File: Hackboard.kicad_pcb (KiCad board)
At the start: 4 copper layers, 110.2 x 55.9 mm, 74 parts, among them J1 Conn_01x31_Socket, J2 Micro_SD_Card, J3 Conn_01x31_Socket, J5 Conn_02x02_Counter_Clockwise, J6 USB_C_Receptacle_USB2.0_16P, J7 Barrel_Jack_Switch, Q1 NMOS, Q2 NMOS, Q3 NMOS, SW1 SW_SPST, U1 NCP164CSN330T1G, U2 AP63205WU, U3 STM32L476RGT6, U4 74LVC4245APW, U5 74LVC4245APW, U6 74LVC4245APW, U7 USBLC6-2SC6, U8 74LVC4245APW, U9 74LVC4245APW

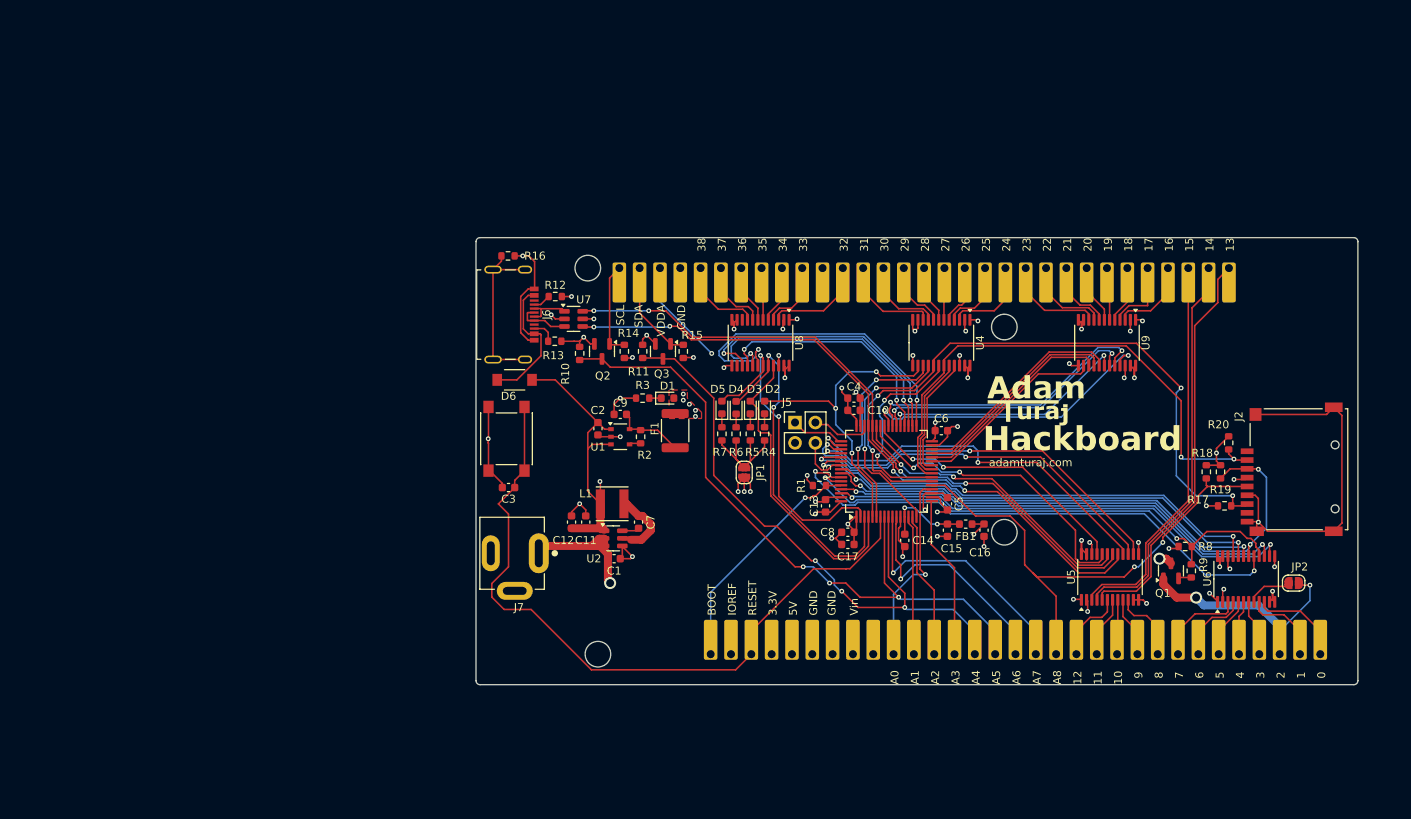
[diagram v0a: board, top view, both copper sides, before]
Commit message: Finish up updated schematic, start outlining border
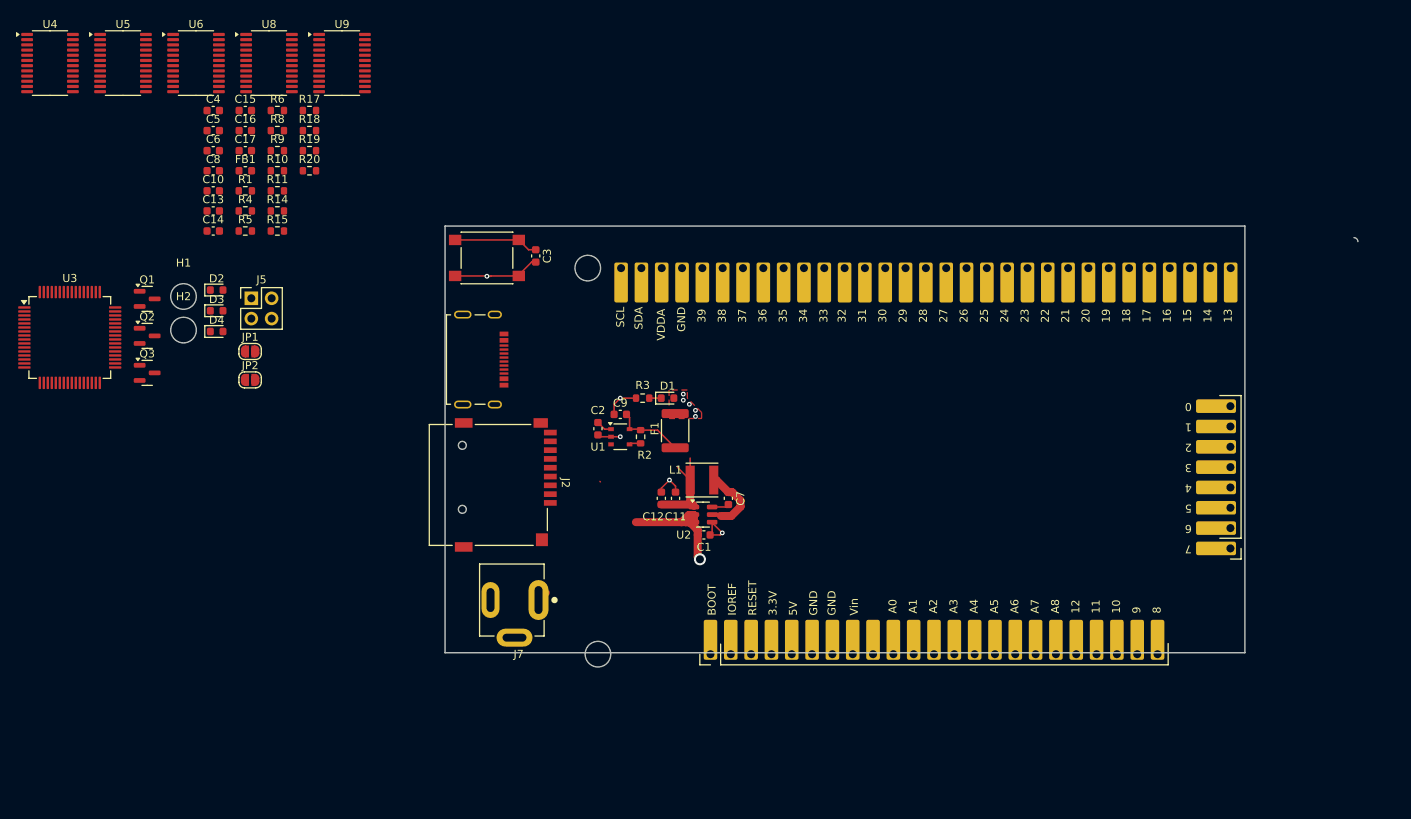
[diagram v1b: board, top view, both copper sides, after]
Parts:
- removed D5: LED, LED_SMD:LED_0603_1608Metric
- removed D6: D_Schottky, DO-221AC:VSSAF3L63HM3
- removed G***: LOGO, Symbol:logo
- removed R12, R13: 5k1, Resistor_SMD:R_0603_1608Metric
- removed R16: 1M, Resistor_SMD:R_0603_1608Metric
- removed R7: 220R, Resistor_SMD:R_0603_1608Metric
- removed REF**: OSHW-Logo2_7.3x6mm_SilkScreen, Symbol:OSHW-Logo2_7.3x6mm_SilkScreen
- removed REF**: KiCad-Logo2_5mm_SilkScreen, Symbol:KiCad-Logo2_5mm_SilkScreen
- removed U7: USBLC6-2SC6, Package_TO_SOT_SMD:SOT-23-6
- added J4: Conn_01x08_Socket, Connector_PinHeader_2.54mm:PinHeader_1x08_P2.54mm_Vertical, F.Cu at (181.1, 102.9)
- J1: value Conn_01x31_Socket -> Conn_01x23_Socket; footprint Connector_PinHeader_2.54mm:PinHeader_1x31_P2.54mm_Vertical -> Connector_PinHeader_2.54mm:PinHeader_1x23_P2.54mm_Vertical
- moved U6 146.3 mm to (51.8, 42.2), turned to 0 degrees
- moved U5 139.1 mm to (42.6, 42.2), turned to 0 degrees
- moved JP2 132.9 mm to (58.5, 81.8)
- moved Q1 132.4 mm to (45.7, 71.7), turned to 0 degrees
- moved R9 125.7 mm to (61.9, 53.1), turned to 0 degrees
- moved R8 124.8 mm to (61.9, 50.6), turned to 0 degrees
- moved R17 124.6 mm to (66.0, 48.1)
- moved R19 120.7 mm to (66.0, 53.1), turned to 0 degrees
- moved R18 119.9 mm to (66.0, 50.6), turned to 0 degrees
- moved R20 119.8 mm to (66.0, 55.6), turned to 0 degrees
- moved U4 116.8 mm to (33.5, 42.2), turned to 0 degrees
- moved H1 106.8 mm to (50.2, 71.4)
- moved C16 105.0 mm to (57.9, 50.6), turned to 0 degrees
- moved U3 103.4 mm to (36.0, 76.5), turned to 0 degrees
- moved C5 103.0 mm to (53.9, 50.6), turned to 0 degrees
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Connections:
- D2 pad 2: LED_PIN31 -> GPIO_34
- D3 pad 2: LED_PIN32 -> GPIO_33
- D4 pad 2: LED_PIN33 -> GPIO_32
- J1 pad 18: SD_SCK_DAC_A8 -> DAC_A8
- J1 pad 19: USB_DN_PIN12_O -> PWM_12_O
- J1 pad 20: USB_DP_PIN11_O -> SD_MISO_11_O
- J1 pad 21: PWM_PIN10_O -> SD_MOSI_10_O
- J1 pad 22: UART_TX_PIN9_O -> SD_CS_9_O
- J1 pad 23: UART_RX_PIN8_O -> GPIO_8_O
- J2 pad 2: SD_CS_PWM_26 -> SD_CS_9
- J2 pad 3: SD_MOSI_GPIO_PIN4 -> SD_MOSI_10
- J2 pad 5: SD_SCK_DAC_A8 -> SD_SCK_24
- J2 pad 7: SD_MISO_PWM_28 -> SD_MISO_11
- J3 pad 10: LED_PIN33_O -> GPIO_34_O
- J3 pad 11: unconnected-(J3-Pin_11-Pad11) -> GPIO_33_O
- J3 pad 12: LED_PIN32_O -> GPIO_32_O
- J3 pad 13: LED_PIN31_O -> GPIO_31_O
- J3 pad 14: GPIO_PIN30_O -> CAN_TX_30_O
- J3 pad 15: PWM_PIN29_O -> CAN_RX_29_O
- J3 pad 17: PWM_PIN27_O -> PWM_27_O
- J3 pad 19: GPIO_PIN25_O -> PWM_25_O
- J3 pad 20: PWM_PIN24_O -> SD_SCK_24_O
- J3 pad 21: PWM_PIN23_O -> GPIO_23_O
- J3 pad 22: GPIO_PIN22_O -> GPIO_22_O
- J3 pad 23: PWM_PIN21_O -> UART_RX_21_O
- J3 pad 24: PWM_PIN20_O -> UART_TX_20_O
- J3 pad 25: PWM_PIN19_O -> PWM_19_O
- J3 pad 26: PWM_PIN18_O -> USB_DP_18_O
- J3 pad 27: PWM_PIN17_O -> USB_DM_17_O
- J3 pad 28: PWM_PIN16_O -> PWM_16_O
- J3 pad 29: PWM_PIN15_O -> PWM_15_O
- J3 pad 30: PWM_PIN14_O -> PWM_14_O
- J3 pad 31: PWM_PIN13_O -> PWM_13_O
- J3 pad 5: SPI_SCK_PIN38_O -> GPIO_39_O
- J3 pad 6: SPI_MOSI_PIN37_O -> SPI_SCK_38_O
- J3 pad 7: SPI_MISO_PIN36_O -> SPI_MOSI_37_O
- J3 pad 8: SPI_CS_PIN35_O -> SPI_MISO_36_O
- J3 pad 9: LED_PIN34_O -> SPI_CS_PWM_35_O
- J5 pad 4: SW_SWO -> SD_SCK_24
- JP2 pad 1: Net-(JP2-A) -> PWM_28_O
- JP2 pad 2: PWM_PIN2_O -> Net-(JP2-B)
- Q1 pad 1: PWM_PIN2_O -> PWM_28_O
- R17 pad 2: SD_MISO_PWM_28 -> SD_MISO_11
- R18 pad 2: SD_SCK_DAC_A8 -> SD_SCK_24
- R19 pad 2: SD_MOSI_GPIO_PIN4 -> SD_MOSI_10
- R20 pad 2: SD_CS_PWM_26 -> SD_CS_9
- R8 pad 1: PWM_PIN2 -> PWM_28
- R9 pad 2: PWM_PIN2 -> PWM_28
- U3 pad 16: PWM_PIN29 -> PWM_12
- U3 pad 2: LED_PIN34 -> GPIO_31
- U3 pad 21: SD_SCK_DAC_A8 -> DAC_A8
- U3 pad 22: SD_MISO_PWM_28 -> SD_MISO_11
- U3 pad 23: PWM_PIN27 -> SD_MOSI_10
- U3 pad 24: SD_CS_PWM_26 -> SD_CS_9
- U3 pad 25: GPIO_PIN25 -> GPIO_8
- U3 pad 26: PWM_PIN24 -> PWM_7
- U3 pad 27: PWM_PIN23 -> PWM_6
- U3 pad 28: GPIO_PIN22 -> GPIO_5
- U3 pad 29: PWM_PIN21 -> PWM_4
- U3 pad 3: LED_PIN33 -> GPIO_32
- U3 pad 30: PWM_PIN20 -> PWM_3
- U3 pad 33: SPI_CS_PIN35 -> PWM_2
- U3 pad 34: SPI_SCK_PIN38 -> SPI_SCK_38
- U3 pad 35: SPI_MISO_PIN36 -> SPI_MISO_36
- U3 pad 36: SPI_MOSI_PIN37 -> SPI_MOSI_37
- U3 pad 37: PWM_PIN19 -> SPI_CS_PWM_35
- U3 pad 38: PWM_PIN18 -> PWM_1
- U3 pad 39: PWM_PIN17 -> PWM_0
- U3 pad 4: LED_PIN32 -> GPIO_33
- U3 pad 40: PWM_PIN16 -> PWM_15
- U3 pad 41: PWM_PIN15 -> PWM_14
- U3 pad 42: PWM_PIN14 -> PWM_13
- U3 pad 43: PWM_PIN13 -> PWM_16
- U3 pad 44: USB_DN_PIN12 -> USB_DM_17
- U3 pad 45: USB_DP_PIN11 -> USB_DP_18
- U3 pad 5: LED_PIN31 -> GPIO_34
- U3 pad 50: PWM_PIN10 -> PWM_19
- U3 pad 51: UART_TX_PIN9 -> UART_TX_20
- U3 pad 52: UART_RX_PIN8 -> UART_RX_21
- U3 pad 53: GPIO_PIN7 -> GPIO_22
- U3 pad 54: GPIO_PIN6 -> GPIO_23
- U3 pad 55: SW_SWO -> SD_SCK_24
- U3 pad 56: PWM_PIN5 -> PWM_25
- U3 pad 57: SD_MOSI_GPIO_PIN4 -> PWM_26
- U3 pad 58: PWM_PIN3 -> PWM_27
- U3 pad 59: PWM_PIN2 -> PWM_28
- U3 pad 6: GPIO_PIN30 -> GPIO_39
- U3 pad 61: CAN_RX_PIN1 -> CAN_RX_29
- U3 pad 62: CAN_TX_PIN0 -> CAN_TX_30
- U4 pad 10: LED_PIN31_O -> GPIO_39_O
- U4 pad 12: LED_PIN31 -> GPIO_39
- U4 pad 13: GPIO_PIN30 -> SPI_SCK_38
- U4 pad 14: PWM_PIN29 -> SPI_MOSI_37
- U4 pad 15: SD_MISO_PWM_28 -> SPI_MISO_36
- U4 pad 16: PWM_PIN27 -> SPI_CS_PWM_35
- U4 pad 17: SD_CS_PWM_26 -> GPIO_34
- U4 pad 18: GPIO_PIN25 -> GPIO_33
- U4 pad 19: PWM_PIN24 -> GPIO_32
- U4 pad 3: PWM_PIN24_O -> GPIO_32_O
- U4 pad 4: GPIO_PIN25_O -> GPIO_33_O
- U4 pad 5: PWM_26_O -> GPIO_34_O
- U4 pad 6: PWM_PIN27_O -> SPI_CS_PWM_35_O
- U4 pad 7: PWM_28_O -> SPI_MISO_36_O
- U4 pad 8: PWM_PIN29_O -> SPI_MOSI_37_O
- U4 pad 9: GPIO_PIN30_O -> SPI_SCK_38_O
- U5 pad 10: UART_RX_PIN8_O -> GPIO_31_O
- U5 pad 12: UART_RX_PIN8 -> GPIO_31
- U5 pad 13: UART_TX_PIN9 -> CAN_TX_30
- U5 pad 14: PWM_PIN10 -> CAN_RX_29
- U5 pad 15: USB_DP_PIN11 -> PWM_28
- U5 pad 16: USB_DN_PIN12 -> PWM_27
- U5 pad 17: PWM_PIN13 -> PWM_26
- U5 pad 18: PWM_PIN14 -> PWM_25
- U5 pad 19: PWM_PIN15 -> SD_SCK_24
- U5 pad 3: PWM_PIN15_O -> SD_SCK_24_O
- U5 pad 4: PWM_PIN14_O -> PWM_25_O
- U5 pad 5: PWM_PIN13_O -> PWM_26_O
- U5 pad 6: USB_DN_PIN12_O -> PWM_27_O
- U5 pad 7: USB_DP_PIN11_O -> Net-(JP2-B)
- U5 pad 8: PWM_PIN10_O -> CAN_RX_29_O
- U5 pad 9: UART_TX_PIN9_O -> CAN_TX_30_O
- U6 pad 10: CAN_TX_PIN0_O -> GPIO_23_O
- U6 pad 12: CAN_TX_PIN0 -> GPIO_23
- U6 pad 13: CAN_RX_PIN1 -> GPIO_22
- U6 pad 14: PWM_PIN2 -> UART_RX_21
- U6 pad 15: PWM_PIN3 -> UART_TX_20
- U6 pad 16: SD_MOSI_GPIO_PIN4 -> PWM_19
- U6 pad 17: PWM_PIN5 -> USB_DP_18
- U6 pad 18: GPIO_PIN6 -> USB_DM_17
- U6 pad 19: GPIO_PIN7 -> PWM_16
- U6 pad 3: GPIO_PIN7_O -> PWM_16_O
- U6 pad 4: GPIO_PIN6_O -> USB_DM_17_O
- U6 pad 5: PWM_PIN5_O -> USB_DP_18_O
- U6 pad 6: GPIO_PIN4_O -> PWM_19_O
- U6 pad 7: PWM_PIN3_O -> UART_TX_20_O
- U6 pad 8: Net-(JP2-A) -> UART_RX_21_O
- U6 pad 9: CAN_RX_PIN1_O -> GPIO_22_O
- U8 pad 10: unconnected-(U8-A7-Pad10) -> PWM_13_O
- U8 pad 12: unconnected-(U8-B7-Pad12) -> PWM_13
- U8 pad 13: SPI_SCK_PIN38 -> PWM_14
- U8 pad 14: SPI_MOSI_PIN37 -> PWM_15
- U8 pad 15: SPI_MISO_PIN36 -> PWM_0
- U8 pad 16: SPI_CS_PIN35 -> PWM_1
- U8 pad 17: LED_PIN34 -> PWM_2
- U8 pad 18: LED_PIN33 -> PWM_3
- U8 pad 19: LED_PIN32 -> PWM_4
- U8 pad 3: LED_PIN32_O -> PWM_4_O
- U8 pad 4: LED_PIN33_O -> PWM_3_O
- U8 pad 5: LED_PIN34_O -> PWM_2_O
- U8 pad 6: SPI_CS_PIN35_O -> PWM_1_O
- U8 pad 7: SPI_MISO_PIN36_O -> PWM_0_O
- U8 pad 8: SPI_MOSI_PIN37_O -> PWM_15_O
- U8 pad 9: SPI_SCK_PIN38_O -> PWM_14_O
- U9 pad 10: PWM_PIN23_O -> GPIO_5_O
- U9 pad 12: PWM_PIN23 -> GPIO_5
- U9 pad 13: GPIO_PIN22 -> PWM_6
- U9 pad 14: PWM_PIN21 -> PWM_7
- U9 pad 15: PWM_PIN20 -> GPIO_8
- U9 pad 16: PWM_PIN19 -> SD_CS_9
- U9 pad 17: PWM_PIN18 -> SD_MOSI_10
- U9 pad 18: PWM_PIN17 -> SD_MISO_11
- U9 pad 19: PWM_PIN16 -> PWM_12
- U9 pad 3: PWM_PIN16_O -> PWM_12_O
- U9 pad 4: PWM_PIN17_O -> SD_MISO_11_O
- U9 pad 5: PWM_PIN18_O -> SD_MOSI_10_O
- U9 pad 6: PWM_PIN19_O -> SD_CS_9_O
- U9 pad 7: PWM_PIN20_O -> GPIO_8_O
- U9 pad 8: PWM_PIN21_O -> PWM_7_O
- U9 pad 9: GPIO_PIN22_O -> PWM_6_O
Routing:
- net GND: track 157.7 -> 27.1 mm, vias 41 -> 5
- net I2C_SCL_A5: track 85.3 -> 0.00 mm, vias 3 -> 0
- net USB_DP_PIN11: track 85.0 -> 0.00 mm, vias 4 -> 0
- net SD_MISO_PWM_28: track 84.5 -> 0.00 mm, vias 4 -> 0
- net USB_DN_PIN12: track 84.3 -> 0.00 mm, vias 4 -> 0
- net RESET: track 90.1 -> 10.6 mm
- net I2C_SDA_A4: track 76.8 -> 0.00 mm, vias 3 -> 0
- net SD_MOSI_GPIO_PIN4: track 73.5 -> 0.00 mm, vias 3 -> 0
- net SD_CS_PWM_26: track 66.9 -> 0.00 mm, vias 2 -> 0
- net PWM_PIN3: track 66.6 -> 0.00 mm, vias 2 -> 0
- net PWM_PIN2: track 65.3 -> 0.00 mm, vias 2 -> 0
- net SD_SCK_DAC_A8: track 64.6 -> 0.00 mm, vias 2 -> 0
- net +3V3: track 65.1 -> 0.85 mm, vias 22 -> 5
- net GPIO_PIN7: track 60.8 -> 0.00 mm, vias 2 -> 0
- net GPIO_PIN6: track 60.0 -> 0.00 mm, vias 2 -> 0
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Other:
- board size 110.2 x 55.9 mm -> 114.1 x 53.3 mm
- board text added: "39"
- board text added: "Copyright (C) 2024 Adam Turaj This program is free software: you can redistribute it and/or modify it under the terms of the GNU General Public License as published by the Free Software Foundation, either version 3 of the License, or (at your option) any later version. This program is distributed in the hope that it will be useful, but WITHOUT ANY WARRANTY; without even the implied warranty of ME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"
- board text removed: "Hackboard"
- board text removed: "adamturaj.com"

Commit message: Finish board layout
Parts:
- added C18: 0.1uF, Capacitor_SMD:C_0603_1608Metric, F.Cu at (99.1, 92.7)
- added D6: D_Schottky, DO-221AC:VSSAF3L63HM3, F.Cu at (94.7, 83.1)
- added R12: 5k1, Resistor_SMD:R_0603_1608Metric, F.Cu at (101.0, 126.5)
- added R13: 5k1, Resistor_SMD:R_0603_1608Metric, F.Cu at (101.0, 129.0)
- added R16: 1M, Resistor_SMD:R_0603_1608Metric, F.Cu at (101.0, 131.5)
- added U7: USBLC6-2SC6, Package_TO_SOT_SMD:SOT-23-6, F.Cu at (95.6, 79.5)
- J5: value Conn_02x02_Counter_Clockwise -> Conn_01x02_Pin; footprint Connector_PinHeader_2.54mm:PinHeader_2x02_P2.54mm_Vertical -> Connector_PinHeader_2.54mm:PinHeader_1x02_P2.54mm_Vertical
- moved U8 113.3 mm to (168.4, 77.9), turned to -90 degrees
- moved U6 110.6 mm to (156.5, 77.9), turned to -90 degrees
- moved U9 110.0 mm to (163.1, 100.8), turned to 90 degrees
- moved U5 105.8 mm to (142.2, 77.9), turned to -90 degrees
- moved H2 102.3 mm to (149.1, 101.9)
- moved H1 99.3 mm to (149.1, 80.3)
- moved U3 92.9 mm to (128.0, 89.2), turned to 90 degrees
- moved Q1 89.2 mm to (134.6, 77.5), turned to -90 degrees
- moved U4 88.8 mm to (114.8, 77.9), turned to -90 degrees
- moved Q2 79.9 mm to (122.3, 99.1)
- moved Q3 79.7 mm to (122.3, 102.8)
- moved JP2 78.0 mm to (136.1, 74.2)
- moved D2 60.4 mm to (112.5, 86.9)
- moved D3 60.3 mm to (112.5, 88.9)
- moved D4 60.1 mm to (112.5, 90.9)
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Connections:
- J5 pad 1: SW_SWCLK -> SW_SWDIO
- J5 pad 2: SW_SWDIO -> SW_SWCLK
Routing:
- net +5V: track 209.3 -> 0.00 mm
- net SD_MOSI_10_O: track 0.00 -> 194.9 mm
- net VCC: track 99.9 -> 0.00 mm, vias 1 -> 0
- net DAC_A0: track 0.00 -> 82.3 mm
- net GND: track 27.1 -> 0.00 mm, vias 5 -> 1
- net RESET: track 10.6 -> 0.00 mm
- net Net-(U2-SW): track 9.29 -> 0.00 mm
- net Net-(U1-OUT): track 8.66 -> 0.00 mm
- net Net-(U2-BST): track 2.16 -> 0.00 mm
- net Net-(D1-K): track 1.50 -> 0.00 mm
- net Net-(U1-PG): track 1.43 -> 0.00 mm
- net +3V3: track 0.85 -> 0.00 mm, vias 5 -> 0
- removed copper zone on F.Cu, net +3V3
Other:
- board size 114.1 x 53.3 mm -> 100 x 53.3 mm
- board text added: "ON"

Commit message: Adjust pinout
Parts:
- moved C16 83.2 mm to (159.3, 115.2), turned to 90 degrees
- moved C15 81.1 mm to (152.4, 114.4)
- moved C4 78.9 mm to (160.8, 103.0), turned to -90 degrees
- moved FB1 77.1 mm to (157.0, 114.4)
- moved C17 75.8 mm to (158.0, 109.6), turned to -90 degrees
- moved C6 74.1 mm to (159.3, 103.0), turned to -90 degrees
- moved R1 73.5 mm to (126.7, 125.8), turned to -90 degrees
- moved C14 72.7 mm to (154.7, 115.1), turned to 90 degrees
- moved C5 72.2 mm to (141.2, 110.6), turned to 90 degrees
- moved C13 67.2 mm to (144.5, 113.1), turned to 180 degrees
- moved C10 66.3 mm to (142.8, 110.6), turned to 90 degrees
- moved R18 65.9 mm to (116.3, 111.8), turned to 180 degrees
- moved R11 62.9 mm to (135.1, 113.8), turned to -90 degrees
- moved R10 62.4 mm to (135.1, 110.7), turned to -90 degrees
- moved R8 62.1 mm to (160.0, 90.9), turned to 90 degrees
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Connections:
- net CAN_RX_29_O renamed PWM_29_O
- net CAN_TX_30_O renamed PWM_30_O
- net GPIO_31_O renamed SD_SCK_31_O
- net PWM_25_O renamed CAN_TX_25_O
- net PWM_26_O renamed CAN_RX_26_O
- net SD_SCK_24_O renamed GPIO_24_O
- JP2 pad 1: PWM_28_O -> PWM_27_O
- Q2 pad 2: +3V3 -> VDDA
- Q3 pad 2: +3V3 -> VDDA
- R10 pad 2: +3V3 -> VDDA
- R11 pad 1: +3V3 -> VDDA
- U3 pad 2: GPIO_31 -> GPIO_24
- U3 pad 55: SD_SCK_24 -> SD_SCK_31
- U3 pad 56: PWM_25 -> PWM_30
- U3 pad 57: PWM_26 -> PWM_29
- U3 pad 58: PWM_27 -> PWM_28
- U3 pad 59: PWM_28 -> PWM_27
- U3 pad 61: CAN_RX_29 -> CAN_RX_26
- U3 pad 62: CAN_TX_30 -> CAN_TX_25
- U5 pad 12: GPIO_31 -> SD_SCK_31
- U5 pad 13: CAN_TX_30 -> PWM_30
- U5 pad 14: CAN_RX_29 -> PWM_29
- U5 pad 17: PWM_26 -> CAN_RX_26
- U5 pad 18: PWM_25 -> CAN_TX_25
- U5 pad 19: SD_SCK_24 -> GPIO_24
- U5 pad 6: PWM_27_O -> Net-(JP2-B)
- U5 pad 7: Net-(JP2-B) -> PWM_28_O
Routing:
- net SW_SWDIO: track 0.00 -> 82.3 mm
- net DAC_A0: track 82.3 -> 0.00 mm
- net VDDA: track 36.8 -> 0.00 mm
- net SCL: track 0.00 -> 36.8 mm

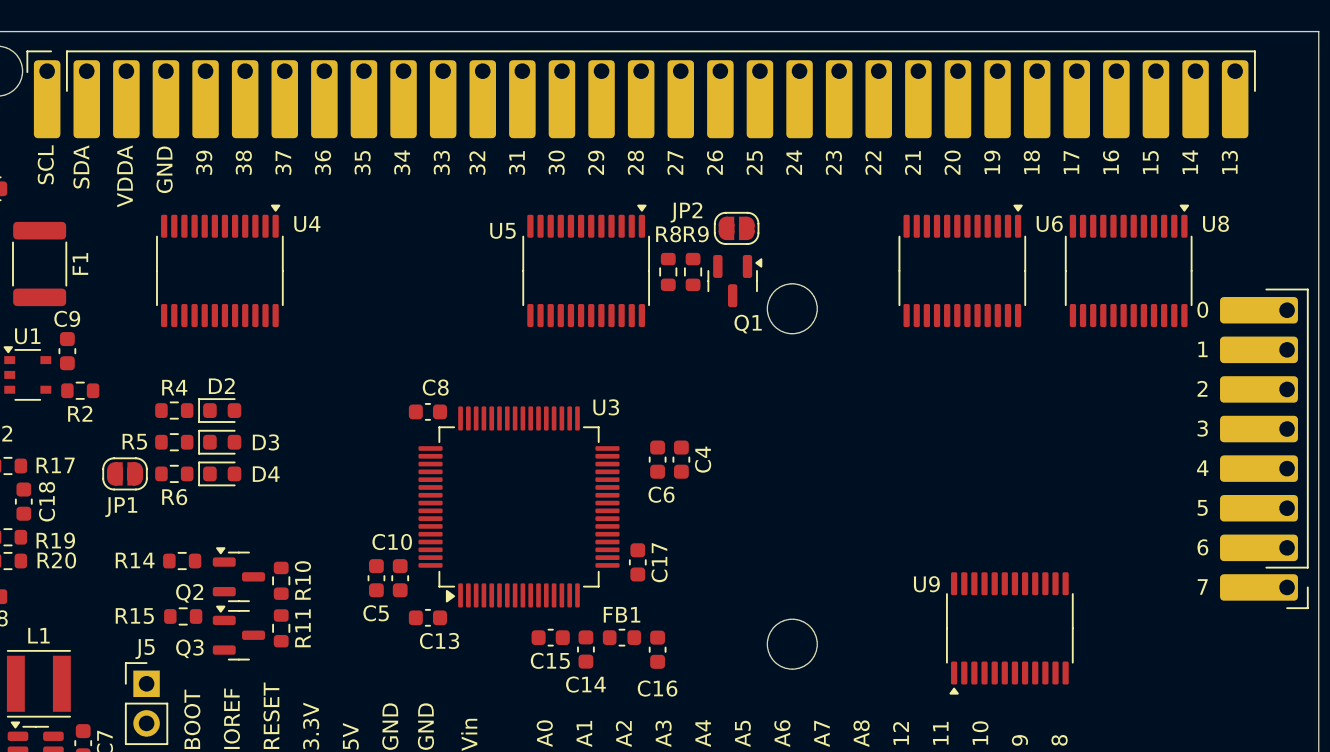
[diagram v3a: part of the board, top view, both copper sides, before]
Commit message: Finish tracing most digital lines
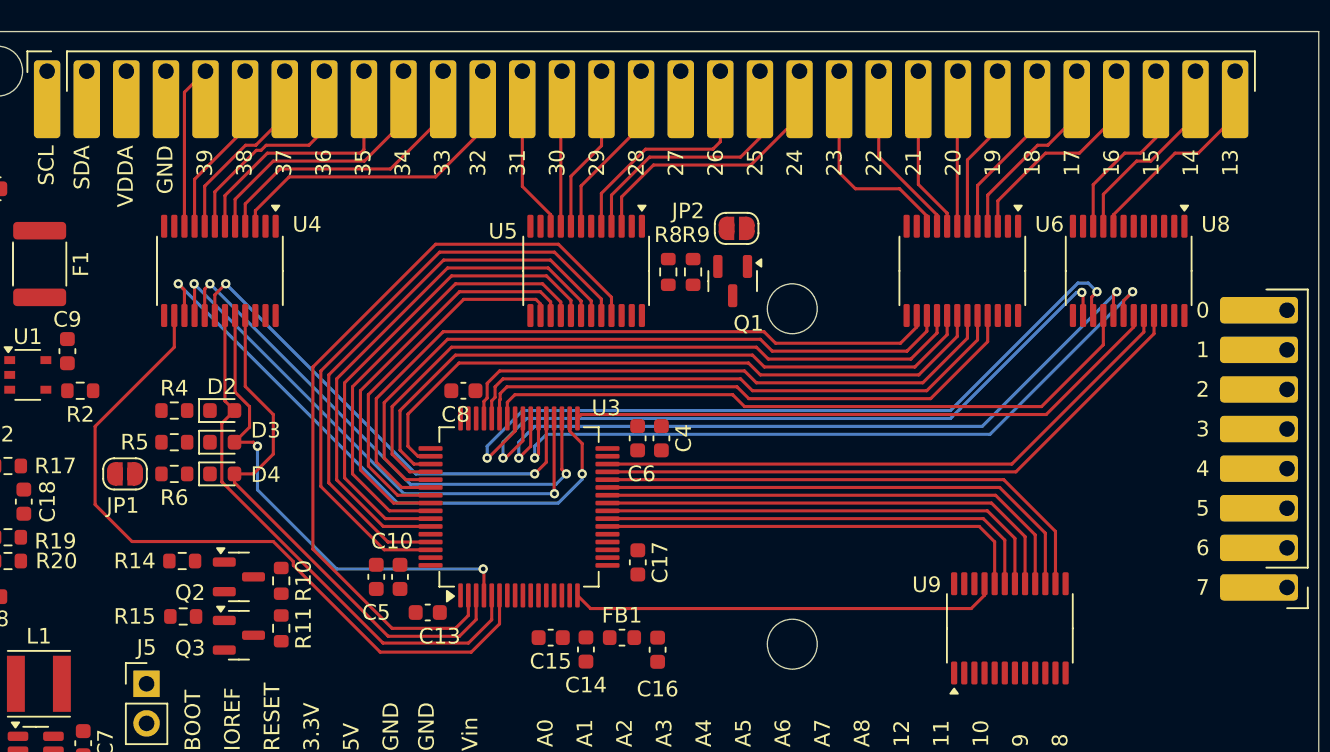
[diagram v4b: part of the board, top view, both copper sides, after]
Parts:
- moved C8 2.65 mm to (146.8, 98.6), turned to 0 degrees
- moved C4 1.88 mm to (159.5, 101.6)
- moved C6 1.88 mm to (158.0, 101.6)
- moved C13 0.34 mm to (144.5, 112.8)
- moved C10 0.09 mm to (142.7, 110.5)
- moved C5 0.09 mm to (141.2, 110.5)
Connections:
- U8 pad 10: PWM_13_O -> PWM_15_O
- U8 pad 12: PWM_13 -> PWM_15
- U8 pad 14: PWM_15 -> PWM_13
- U8 pad 8: PWM_15_O -> PWM_13_O
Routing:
- net SD_MOSI_10_O: track 194.9 -> 0.00 mm
- net SW_SWDIO: track 82.3 -> 0.00 mm
- net GPIO_24: track 0.00 -> 50.4 mm
- net PWM_14: track 0.00 -> 49.5 mm, vias 0 -> 2
- net PWM_0: track 0.00 -> 47.8 mm, vias 0 -> 2
- net PWM_1: track 0.00 -> 47.6 mm, vias 0 -> 2
- net PWM_15: track 0.00 -> 46.8 mm, vias 0 -> 2
- net GPIO_39: track 0.00 -> 46.8 mm
- net GPIO_23: track 0.00 -> 46.1 mm
- net GPIO_22: track 0.00 -> 45.4 mm
- net UART_RX_21: track 0.00 -> 44.6 mm
- net UART_TX_20: track 0.00 -> 43.8 mm
- net PWM_13: track 0.00 -> 43.3 mm
- net PWM_19: track 0.00 -> 43.0 mm
- net PWM_4: track 0.00 -> 39.9 mm
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
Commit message: Finish tracing all pins, start tracing power
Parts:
- moved J5 31.5 mm to (138.9, 88.4)
- moved Q2 4.89 mm to (131.7, 115.3)
- moved R14 4.89 mm to (128.0, 114.3)
- moved R10 4.89 mm to (134.4, 115.6), turned to 90 degrees
- moved Q3 2.53 mm to (131.7, 111.8)
- moved R15 2.53 mm to (128.1, 110.6)
- moved R11 1.48 mm to (134.4, 112.5), turned to 90 degrees
- moved C17 0.67 mm to (158.0, 110.2)
- turned JP2 to 180 degrees
- turned R4 to 180 degrees
- turned R6 to 180 degrees
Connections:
- J2 pad 5: SD_SCK_24 -> SD_SCK_31
- Q1 pad 1: PWM_28_O -> PWM_27_O
- R18 pad 2: SD_SCK_24 -> SD_SCK_31
- R8 pad 1: PWM_28 -> PWM_27
- R9 pad 2: PWM_28 -> PWM_27
- U3 pad 10: ANALOG_A7 -> ANALOG_A6
- U3 pad 11: ANALOG_A6 -> ANALOG_A7
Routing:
- net RESET: track 0.00 -> 111.9 mm, vias 0 -> 2
- net SD_SCK_31: track 23.8 -> 84.9 mm, vias 0 -> 2
- net SD_MOSI_10: track 28.9 -> 81.6 mm, vias 0 -> 2
- net I2C_SDA_A4: track 0.00 -> 51.9 mm, vias 0 -> 1
- net I2C_SCL_A5: track 0.00 -> 48.0 mm, vias 0 -> 1
- net SD_MISO_11: track 27.9 -> 73.9 mm, vias 0 -> 2
- net SD_CS_9: track 29.8 -> 75.2 mm, vias 0 -> 2
- net SCL: track 0.00 -> 43.7 mm
- net SDA: track 0.00 -> 40.2 mm
- net +5V: track 0.00 -> 36.8 mm
- net BOOT: track 0.00 -> 31.3 mm, vias 0 -> 1
- net ANALOG_A6: track 0.00 -> 30.7 mm, vias 0 -> 1
- net GND: track 0.00 -> 29.9 mm
- net DAC_A8: track 0.00 -> 29.8 mm
- net ANALOG_A7: track 0.00 -> 28.4 mm, vias 0 -> 1
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- removed copper zone on In2.Cu, net +3V3
- removed copper zone on In1.Cu, net GND
